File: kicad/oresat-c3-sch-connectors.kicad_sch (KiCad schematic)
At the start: 29 parts, among them J1 J-SAMTEC-TFM-120-01-L-D-RA, J2 J-TE-Debug-2-1734592-0, J3 J-MOLEX-SMPM-73300-003X, J4 J-MOLEX-SMPM-73300-003X

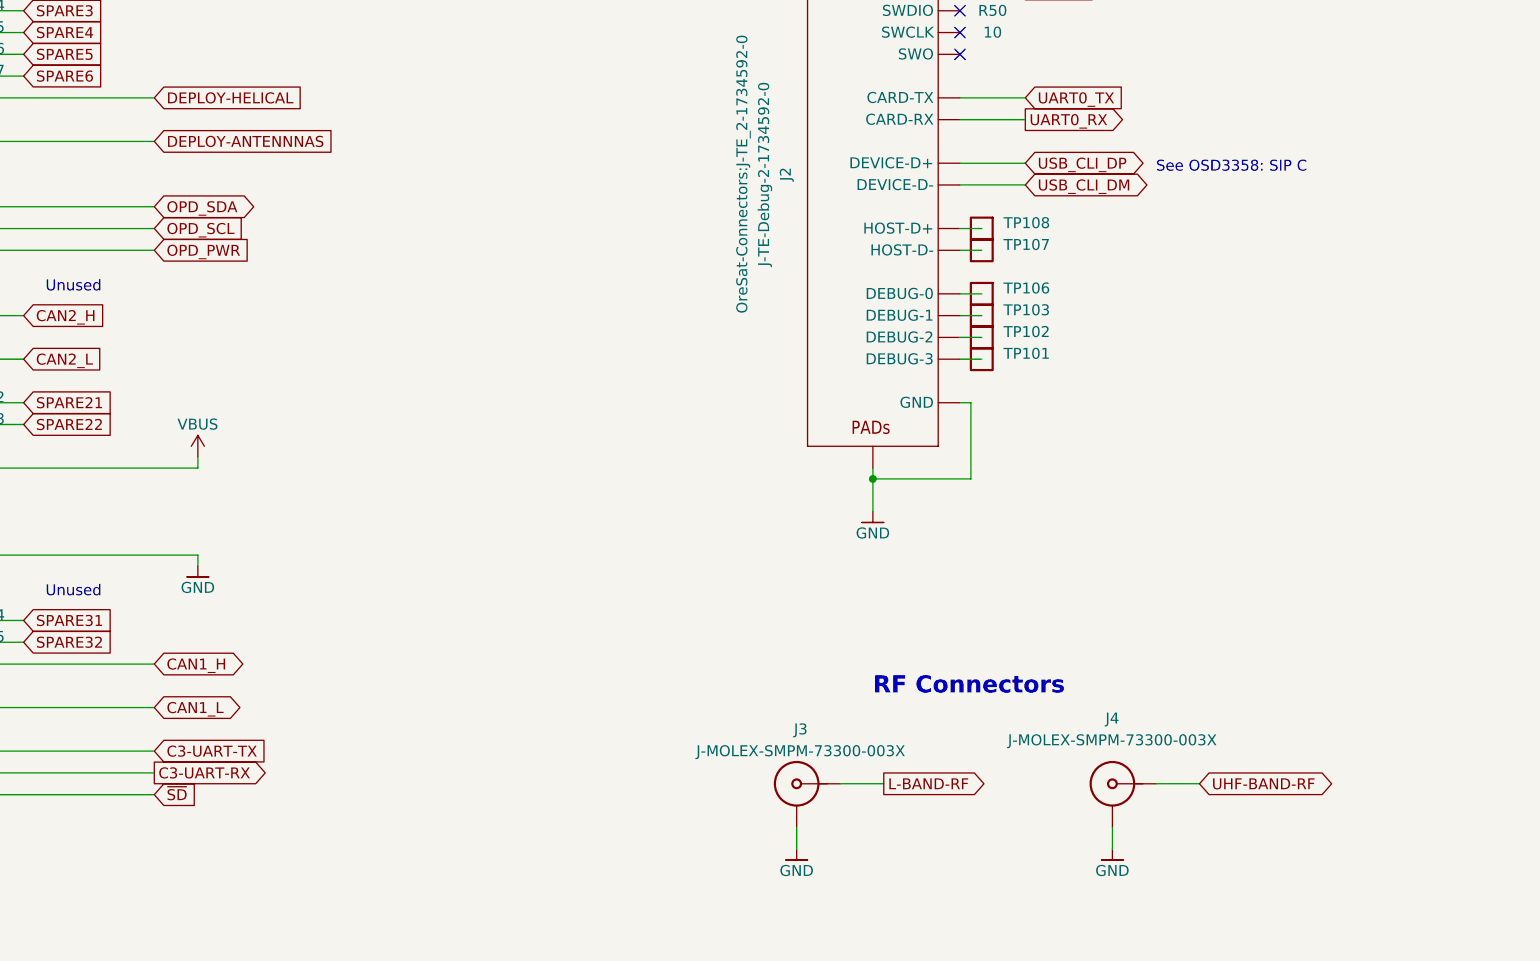
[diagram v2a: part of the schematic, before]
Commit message: Finished UHF radio schematic. Added sheet numbers to external labels. Still to do: L band radio, hooking up GPIO to the OSD3358, and test points.
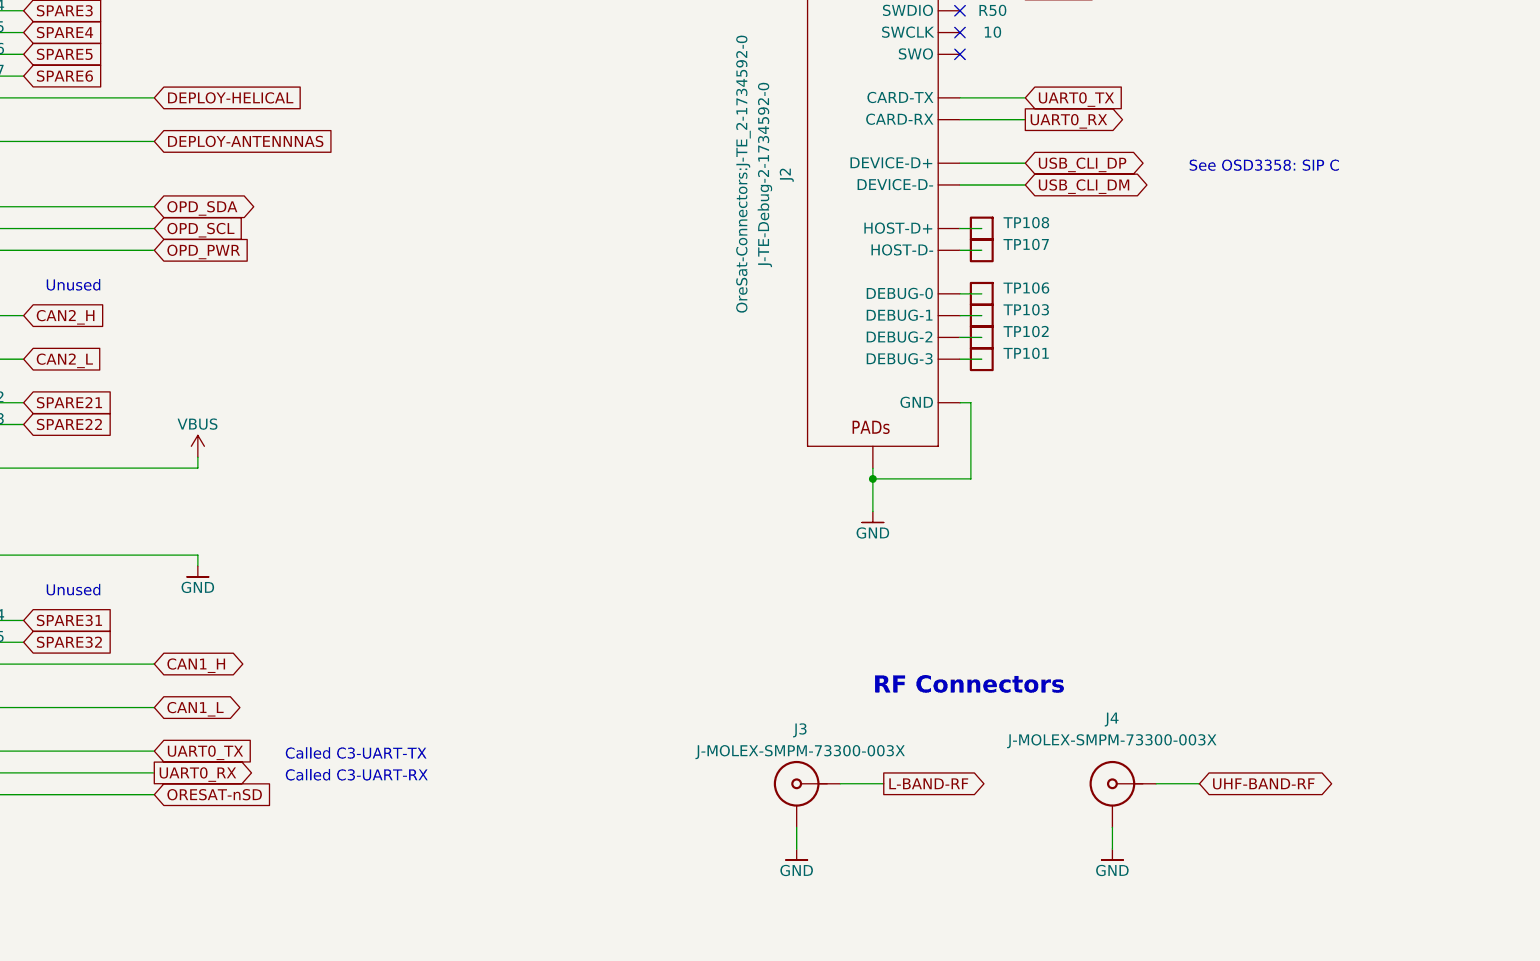
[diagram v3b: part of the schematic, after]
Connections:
- net C3-UART-RX is gone; now on net UART0_RX: J1.38
- net C3-UART-TX is gone; now on net UART0_TX: J1.37
- net ~{SD} renamed ORESAT-nSD
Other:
- note added: "Called C3-UART-RX"
- note added: "Called C3-UART-TX"
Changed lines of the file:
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@@
     (effects (font (size 2 2) (thickness 0.4) bold) (justify left bottom))
   )
-  (text "See OSD3358: SIP C" (at 233.68 105.41 0)
+  (text "See OSD3358: SIP C" (at 237.49 105.41 0)
     (effects (font (size 1.27 1.27)) (justify left bottom))
   )
@@
     (effects (font (size 2 2) (thickness 0.4) bold) (justify left bottom))
   )
+  (text "Called C3-UART-TX" (at 132.08 173.99 0)
+    (effects (font (size 1.27 1.27)) (justify left bottom))
+  )
   (text "Oresat Debug Connector" (at 186.69 66.04 0)
     (effects (font (size 2 2) (thickness 0.4) bold) (justify left bottom))
@@
   )
   (text "Unused" (at 104.14 119.38 0)
+    (effects (font (size 1.27 1.27)) (justify left bottom))
+  )
+  (text "Called C3-UART-RX" (at 132.08 176.53 0)
     (effects (font (size 1.27 1.27)) (justify left bottom))
   )
@@
     (effects (font (size 1.27 1.27)) (justify left))
     (property "Intersheetrefs" "${INTERSHEET_REFS}" (at 111.2098 83.7406 0)
-      (effects (font (size 1.27 1.27)) (justify left) hide)
+      (effects (font (size 1.27 1.27)) (justify left))
     )
   )
@@
     (effects (font (size 1.27 1.27)) (justify left))
     (property "Intersheetrefs" "${INTERSHEET_REFS}" (at 111.2098 81.2006 0)
-      (effects (font (size 1.27 1.27)) (justify left) hide)
+      (effects (font (size 1.27 1.27)) (justify left))
     )
   )
@@
     (effects (font (size 1.27 1.27)) (justify left))
     (property "Intersheetrefs" "${INTERSHEET_REFS}" (at 230.3567 96.52 0)
-      (effects (font (size 1.27 1.27)) (justify left) hide)
+      (effects (font (size 1.27 1.27)) (justify left))
     )
   )
@@
     (effects (font (size 1.27 1.27)) (justify left))
     (property "Intersheetrefs" "${INTERSHEET_REFS}" (at 111.2098 93.9006 0)
-      (effects (font (size 1.27 1.27)) (justify left) hide)
+      (effects (font (size 1.27 1.27)) (justify left))
     )
   )
@@
     (effects (font (size 1.27 1.27)) (justify left))
     (property "Intersheetrefs" "${INTERSHEET_REFS}" (at 112.4193 157.4006 0)
-      (effects (font (size 1.27 1.27)) (justify left) hide)
+      (effects (font (size 1.27 1.27)) (justify left))
     )
   )
@@
     (effects (font (size 1.27 1.27)) (justify left))
     (property "Intersheetrefs" "${INTERSHEET_REFS}" (at 230.6591 99.06 0)
-      (effects (font (size 1.27 1.27)) (justify left) hide)
+      (effects (font (size 1.27 1.27)) (justify left))
     )
   )
@@
     (effects (font (size 1.27 1.27)) (justify left))
     (property "Intersheetrefs" "${INTERSHEET_REFS}" (at 110.9074 126.9206 0)
-      (effects (font (size 1.27 1.27)) (justify left) hide)
+      (effects (font (size 1.27 1.27)) (justify left))
     )
   )
@@
     (effects (font (size 1.27 1.27)) (justify left))
     (property "Intersheetrefs" "${INTERSHEET_REFS}" (at 233.8266 106.68 0)
-      (effects (font (size 1.27 1.27)) (justify left) hide)
+      (effects (font (size 1.27 1.27)) (justify left))
     )
   )
@@
     (effects (font (size 1.27 1.27)) (justify left))
     (property "Intersheetrefs" "${INTERSHEET_REFS}" (at 112.4193 159.9406 0)
-      (effects (font (size 1.27 1.27)) (justify left) hide)
+      (effects (font (size 1.27 1.27)) (justify left))
     )
   )
@@
     (effects (font (size 1.27 1.27)) (justify left))
     (property "Intersheetrefs" "${INTERSHEET_REFS}" (at 229.1473 76.2 0)
-      (effects (font (size 1.27 1.27)) (justify left) hide)
+      (effects (font (size 1.27 1.27)) (justify left))
     )
   )
@@
     (effects (font (size 1.27 1.27)) (justify left))
     (property "Intersheetrefs" "${INTERSHEET_REFS}" (at 256.9892 176.53 0)
-      (effects (font (size 1.27 1.27)) (justify left) hide)
+      (effects (font (size 1.27 1.27)) (justify left))
     )
   )
@@
     (effects (font (size 1.27 1.27)) (justify left))
     (property "Intersheetrefs" "${INTERSHEET_REFS}" (at 111.2098 88.8206 0)
-      (effects (font (size 1.27 1.27)) (justify left) hide)
+      (effects (font (size 1.27 1.27)) (justify left))
     )
   )
@@
     (effects (font (size 1.27 1.27)) (justify left))
     (property "Intersheetrefs" "${INTERSHEET_REFS}" (at 228.2399 83.82 0)
-      (effects (font (size 1.27 1.27)) (justify left) hide)
+      (effects (font (size 1.27 1.27)) (justify left))
     )
   )
@@
     (effects (font (size 1.27 1.27)) (justify left))
     (property "Intersheetrefs" "${INTERSHEET_REFS}" (at 111.2098 91.3606 0)
-      (effects (font (size 1.27 1.27)) (justify left) hide)
+      (effects (font (size 1.27 1.27)) (justify left))
     )
   )
@@
     (effects (font (size 1.27 1.27)) (justify left))
     (property "Intersheetrefs" "${INTERSHEET_REFS}" (at 112.4193 134.5406 0)
-      (effects (font (size 1.27 1.27)) (justify left) hide)
+      (effects (font (size 1.27 1.27)) (justify left))
     )
   )
@@
     (effects (font (size 1.27 1.27)) (justify left))
     (property "Intersheetrefs" "${INTERSHEET_REFS}" (at 127.7514 167.64 0)
-      (effects (font (size 1.27 1.27)) (justify left) hide)
-    )
-  )
-  (global_label "C3-UART-TX" (shape input) (at 116.84 172.72 0) (fields_autoplaced)
-    (effects (font (size 1.27 1.27)) (justify left))
-    (property "Intersheetrefs" "${INTERSHEET_REFS}" (at 131.7112 172.6406 0)
-      (effects (font (size 1.27 1.27)) (justify left) hide)
+      (effects (font (size 1.27 1.27)) (justify left))
+    )
+  )
+  (global_label "UART0_TX" (shape input) (at 116.84 172.72 0) (fields_autoplaced)
+    (effects (font (size 1.27 1.27)) (justify left))
+    (property "Intersheetrefs" "${INTERSHEET_REFS}" (at 128.7567 172.72 0)
+      (effects (font (size 1.27 1.27)) (justify left))
     )
   )
@@
     (effects (font (size 1.27 1.27)) (justify left))
     (property "Intersheetrefs" "${INTERSHEET_REFS}" (at 128.0826 114.2206 0)
-      (effects (font (size 1.27 1.27)) (justify left) hide)
+      (effects (font (size 1.27 1.27)) (justify left))
     )
   )
@@
     (effects (font (size 1.27 1.27)) (justify left))
     (property "Intersheetrefs" "${INTERSHEET_REFS}" (at 112.4193 132.0006 0)
-      (effects (font (size 1.27 1.27)) (justify left) hide)
+      (effects (font (size 1.27 1.27)) (justify left))
     )
   )
@@
     (effects (font (size 1.27 1.27)) (justify left))
     (property "Intersheetrefs" "${INTERSHEET_REFS}" (at 129.2633 109.22 0)
-      (effects (font (size 1.27 1.27)) (justify left) hide)
-    )
-  )
-  (global_label "~{SD}" (shape input) (at 116.84 177.8 0) (fields_autoplaced)
-    (effects (font (size 1.27 1.27)) (justify left))
-    (property "Intersheetrefs" "${INTERSHEET_REFS}" (at 121.7326 177.7206 0)
-      (effects (font (size 1.27 1.27)) (justify left) hide)
+      (effects (font (size 1.27 1.27)) (justify left))
+    )
+  )
+  (global_label "ORESAT-nSD" (shape input) (at 116.84 177.8 0) (fields_autoplaced)
+    (effects (font (size 1.27 1.27)) (justify left))
+    (property "Intersheetrefs" "${INTERSHEET_REFS}" (at 131.9619 177.8 0)
+      (effects (font (size 1.27 1.27)) (justify left))
     )
   )
@@
     (effects (font (size 1.27 1.27)) (justify left))
     (property "Intersheetrefs" "${INTERSHEET_REFS}" (at 128.0538 162.56 0)
-      (effects (font (size 1.27 1.27)) (justify left) hide)
+      (effects (font (size 1.27 1.27)) (justify left))
     )
   )
@@
     (effects (font (size 1.27 1.27)) (justify left))
     (property "Intersheetrefs" "${INTERSHEET_REFS}" (at 128.0915 111.76 0)
-      (effects (font (size 1.27 1.27)) (justify left) hide)
+      (effects (font (size 1.27 1.27)) (justify left))
     )
   )
@@
     (effects (font (size 1.27 1.27)) (justify left))
     (property "Intersheetrefs" "${INTERSHEET_REFS}" (at 233.6452 104.14 0)
-      (effects (font (size 1.27 1.27)) (justify left) hide)
-    )
-  )
-  (global_label "C3-UART-RX" (shape output) (at 116.84 175.26 0) (fields_autoplaced)
-    (effects (font (size 1.27 1.27)) (justify left))
-    (property "Intersheetrefs" "${INTERSHEET_REFS}" (at 132.5063 175.26 0)
-      (effects (font (size 1.27 1.27)) (justify left) hide)
+      (effects (font (size 1.27 1.27)) (justify left))
+    )
+  )
+  (global_label "UART0_RX" (shape output) (at 116.84 175.26 0) (fields_autoplaced)
+    (effects (font (size 1.27 1.27)) (justify left))
+    (property "Intersheetrefs" "${INTERSHEET_REFS}" (at 129.0591 175.26 0)
+      (effects (font (size 1.27 1.27)) (justify left))
     )
   )
@@
     (effects (font (size 1.27 1.27)) (justify left))
     (property "Intersheetrefs" "${INTERSHEET_REFS}" (at 216.3264 176.53 0)
-      (effects (font (size 1.27 1.27)) (justify left) hide)
+      (effects (font (size 1.27 1.27)) (justify left))
     )
   )
@@
     (effects (font (size 1.27 1.27)) (justify left))
     (property "Intersheetrefs" "${INTERSHEET_REFS}" (at 139.2797 101.6 0)
-      (effects (font (size 1.27 1.27)) (justify left) hide)
+      (effects (font (size 1.27 1.27)) (justify left))
     )
   )
@@
     (effects (font (size 1.27 1.27)) (justify left))
     (property "Intersheetrefs" "${INTERSHEET_REFS}" (at 111.2098 86.2806 0)
-      (effects (font (size 1.27 1.27)) (justify left) hide)
+      (effects (font (size 1.27 1.27)) (justify left))
     )
   )
@@
     (effects (font (size 1.27 1.27)) (justify left))
     (property "Intersheetrefs" "${INTERSHEET_REFS}" (at 111.2098 121.8406 0)
-      (effects (font (size 1.27 1.27)) (justify left) hide)
+      (effects (font (size 1.27 1.27)) (justify left))
     )
   )
@@
     (effects (font (size 1.27 1.27)) (justify left))
     (property "Intersheetrefs" "${INTERSHEET_REFS}" (at 135.9535 96.52 0)
-      (effects (font (size 1.27 1.27)) (justify left) hide)
-    )
-  )
+      (effects (font (size 1.27 1.27)) (justify left))
+    )
+  )
